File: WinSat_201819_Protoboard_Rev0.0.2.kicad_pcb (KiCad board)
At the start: 4 copper layers, 41 x 62 mm, 63 parts, among them J1 Conn_01x02_Female, J2 Conn_01x02_Female, J3 Conn_01x02_Female, J4 Conn_01x02_Female, J5 Conn_01x03_Female, J6 Conn_01x02_Female, J7 JTAG-6PIN, J8 Conn_01x03_Female, P1 TPS82150, Q1 SSM3K329R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

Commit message: Added GPS JST
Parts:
- added J9: Conn_01x04, Connector_JST:JST_PH_B4B-PH-K_1x04_P2.00mm_Vertical, F.Cu at (87.0, 100.0)
- added MK1: Mounting_Hole, MountingHole:MountingHole_3.2mm_M3, F.Cu at (68.0, 124.0)
- added MK2: Mounting_Hole, MountingHole:MountingHole_3.2mm_M3, F.Cu at (100.5, 70.5)
- added MK3: Mounting_Hole, MountingHole:MountingHole_3.2mm_M3, F.Cu at (101.0, 124.0)
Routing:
- net Net-(J9-Pad2): track 1.27 -> 10.5 mm
- net Net-(J9-Pad1): track 1.71 -> 7.97 mm
- net GND: track 120.6 -> 116.0 mm, vias 62 -> 63
- net +3V3: track 70.0 -> 71.5 mm, vias 20 -> 21

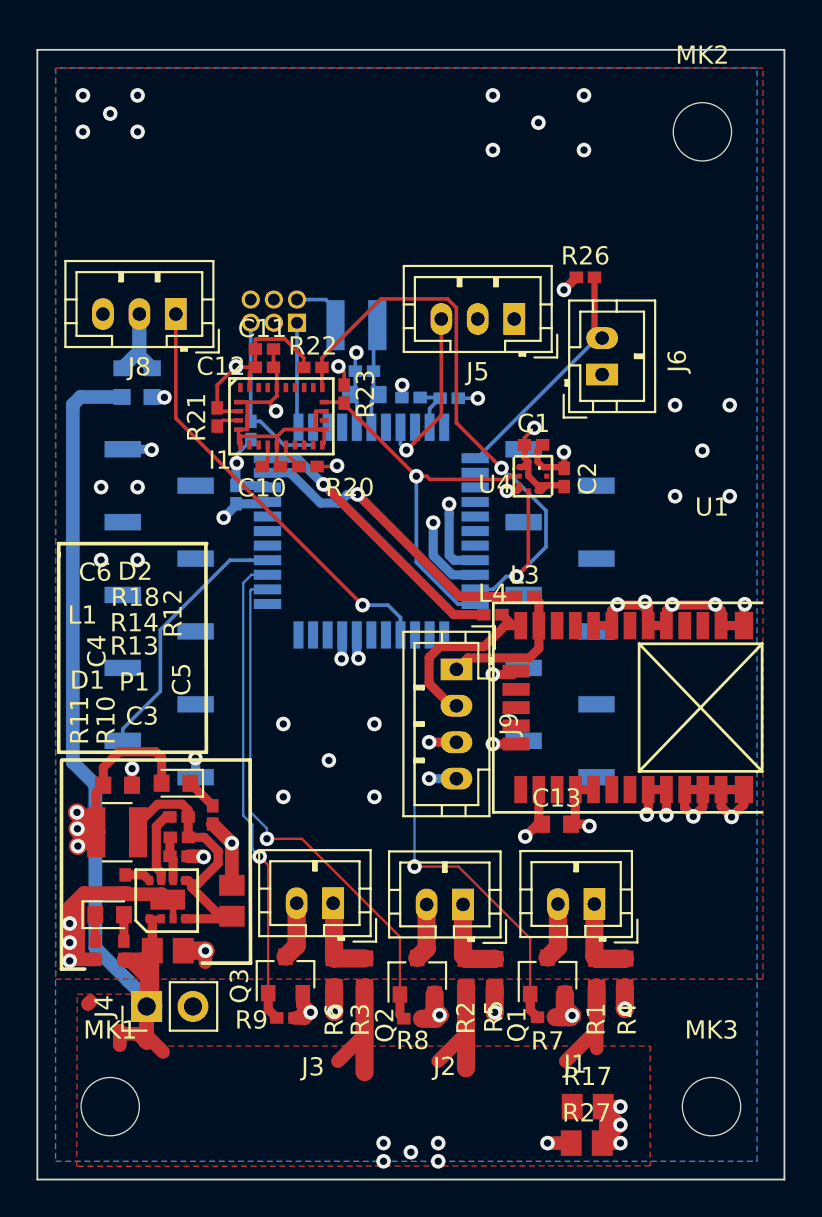
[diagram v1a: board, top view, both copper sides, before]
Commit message: GPS to 3 pin and board shrinkage
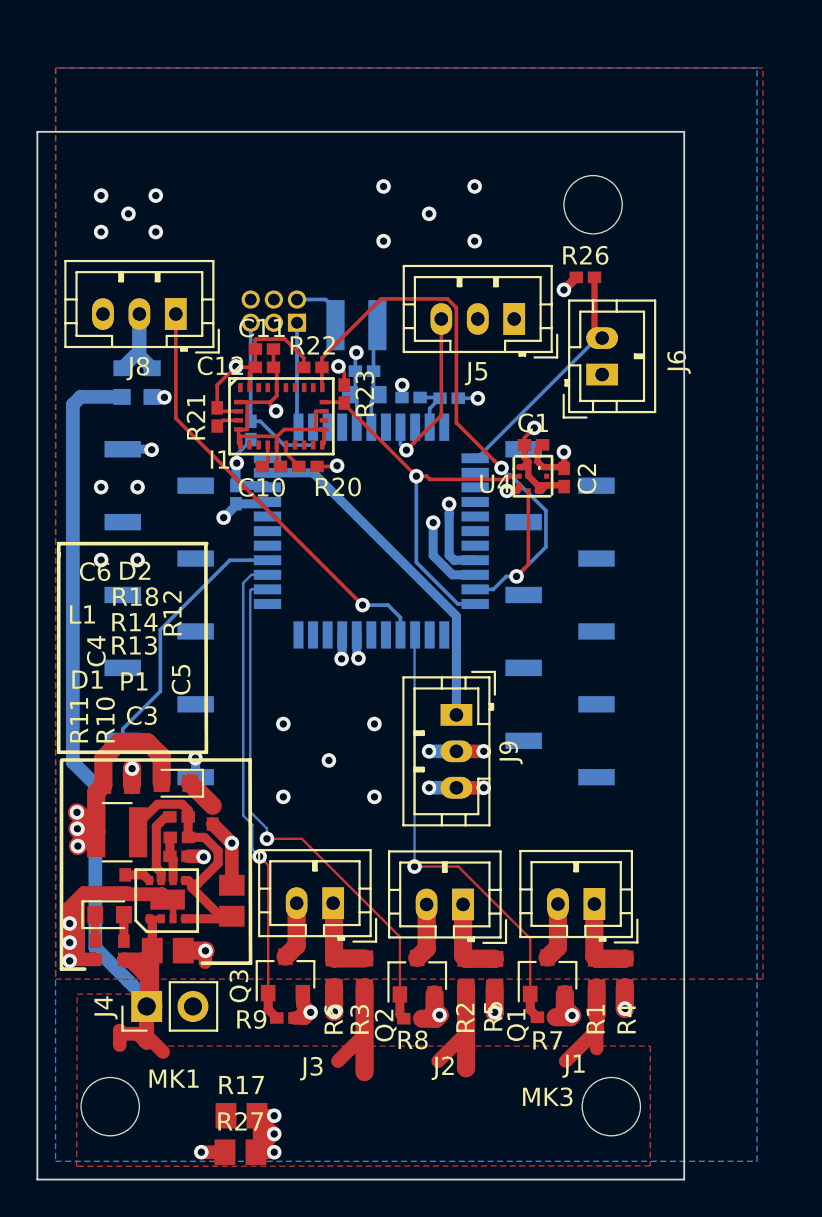
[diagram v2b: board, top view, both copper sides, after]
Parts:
- removed C13: 4.7uF, Capacitor_SMD:C_0603_1608Metric
- removed L3: L_Small, OSD335x-KiCad-master:Not_Broken_0402
- removed L4: BLM15HD102SN1, OSD335x-KiCad-master:Not_Broken_0402
- removed U1: CAM-M8, OSD335x-KiCad-master:CAM-M8
- J9: value Conn_01x04 -> Conn_01x03_Female; footprint Connector_JST:JST_PH_B4B-PH-K_1x04_P2.00mm_Vertical -> Connector_JST:JST_PH_B3B-PH-K_1x03_P2.00mm_Vertical
- moved R17 19.0 mm to (75.2, 124.5)
- moved R27 19.0 mm to (75.2, 126.5)
- moved MK2 7.21 mm to (94.5, 74.5)
- moved MK3 5.50 mm to (95.5, 124.0)
- moved J9 2.50 mm to (87.0, 102.5)
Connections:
- J9 pad 1: Net-(J9-Pad1) -> GPS_TX-MCU_RX
- J9 pad 2: Net-(J9-Pad2) -> GND
- U9 pad 33: GPS_RX-MCU_TX -> Net-(U9-Pad33)
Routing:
- net GND: track 116.0 -> 86.0 mm, vias 63 -> 44
- net GPS_RX-MCU_TX: track 15.4 -> 0.00 mm, vias 1 -> 0
- net Net-(J9-Pad2): track 10.5 -> 0.00 mm
- net Net-(J9-Pad1): track 7.97 -> 0.00 mm
- net +3V3: track 71.5 -> 66.8 mm, vias 21 -> 19
- net GPS_TX-MCU_RX: track 16.8 -> 19.0 mm, vias 1 -> 0
- net Net-(D2-Pad1): track 1.75 -> 3.49 mm
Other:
- board size 41 x 62 mm -> 35.5 x 57.5 mm

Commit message: FTDI Added
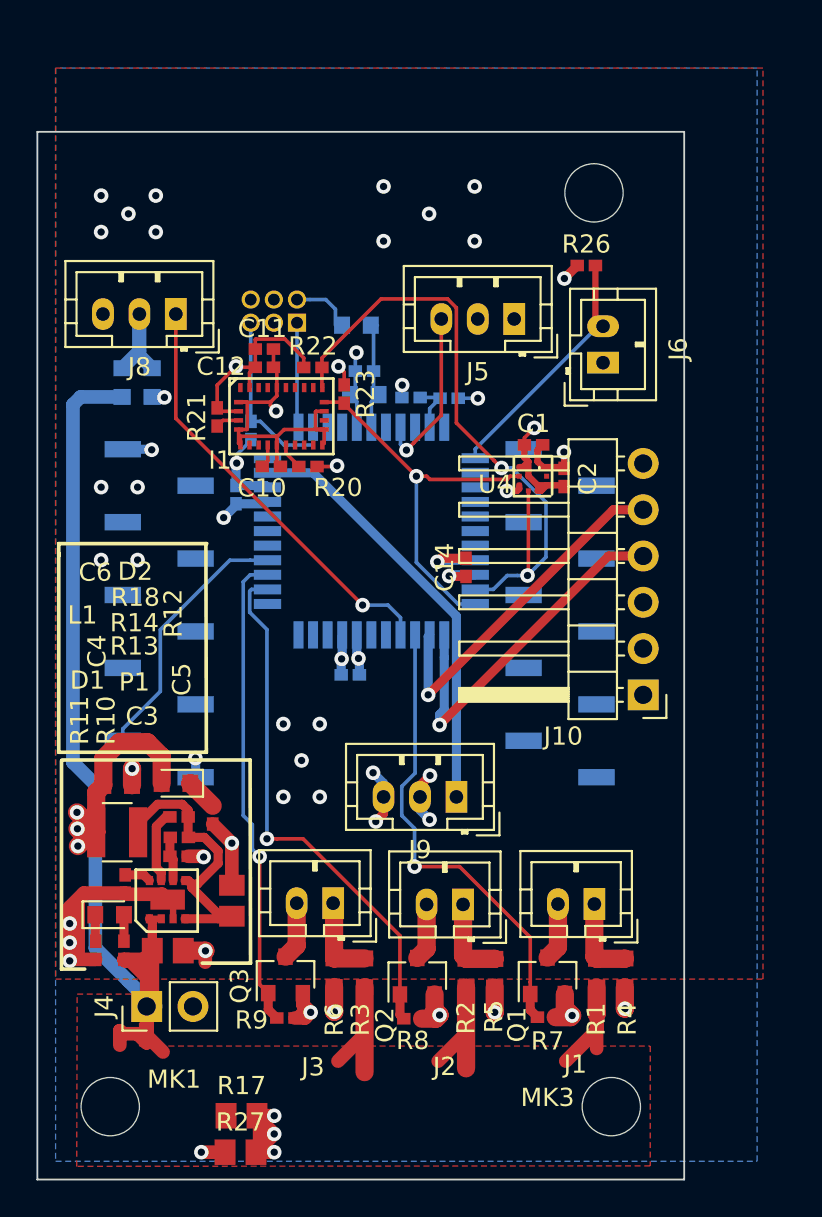
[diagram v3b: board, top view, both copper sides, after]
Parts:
- added C13: C_Small, OSD335x-KiCad-master:Not_Broken_0402, B.Cu at (81.2, 100.3)
- added C14: C_Small, OSD335x-KiCad-master:Not_Broken_0402, F.Cu at (87.5, 94.4)
- added J10: Conn_01x06_Male, Connector_PinHeader_2.54mm:PinHeader_1x06_P2.54mm_Horizontal, F.Cu at (97.2, 101.4)
- L2: value 10uH -> 220OHM 100MHZ; footprint Inductor_SMD:L_Abracon_ASPI-3012S -> Inductor_SMD:L_0603_1608Metric
- moved J9 4.50 mm to (87.0, 107.0), turned to 180 degrees
- moved MK2 0.65 mm to (94.5, 73.8)
- moved R26 0.65 mm to (94.1, 77.8)
- moved J6 0.65 mm to (95.0, 83.2)
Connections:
- U9 pad 12: Net-(U9-Pad12) -> FTDI_OLOG_TX-MCU_RX
- U9 pad 13: Net-(U9-Pad13) -> FTDI_OLOG_RX-MCU_TX
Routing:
- net FTDI_OLOG_TX-MCU_RX: track 0.00 -> 20.1 mm, vias 0 -> 1
- net FTDI_OLOG_RX-MCU_TX: track 0.00 -> 19.3 mm, vias 0 -> 1
- net GPS_TX-MCU_RX: track 19.0 -> 23.5 mm
- net +3V3: track 66.8 -> 65.6 mm
- net TEMP_SENSE-ADC: track 13.2 -> 13.9 mm
- net MOSFET0_GPIO: track 25.2 -> 25.8 mm

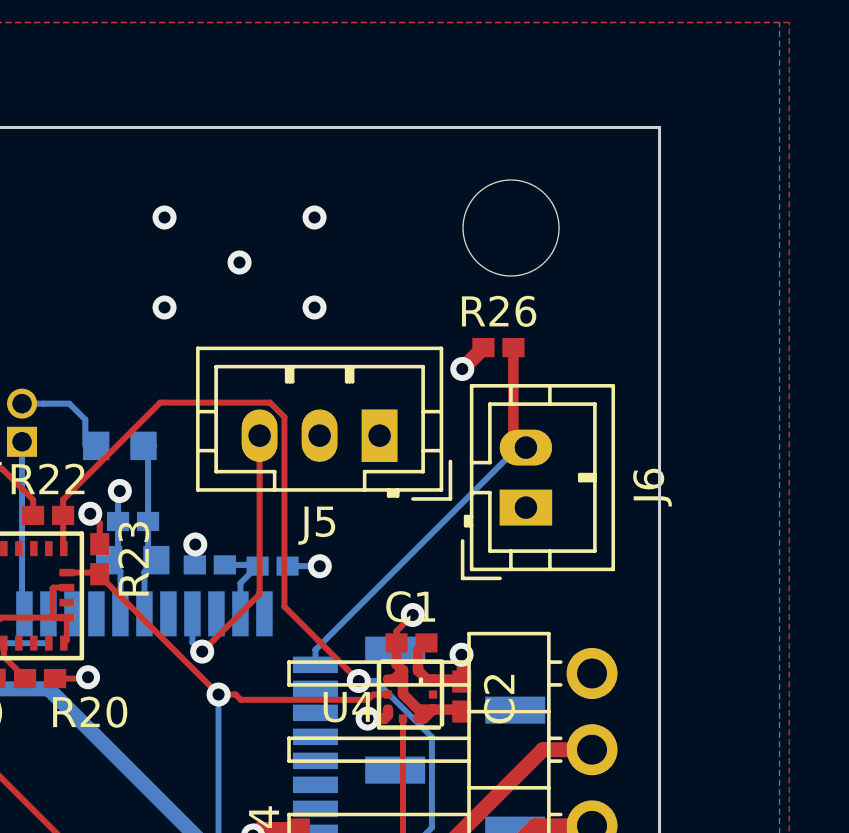
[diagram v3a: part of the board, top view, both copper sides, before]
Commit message: Fix mounting hole position
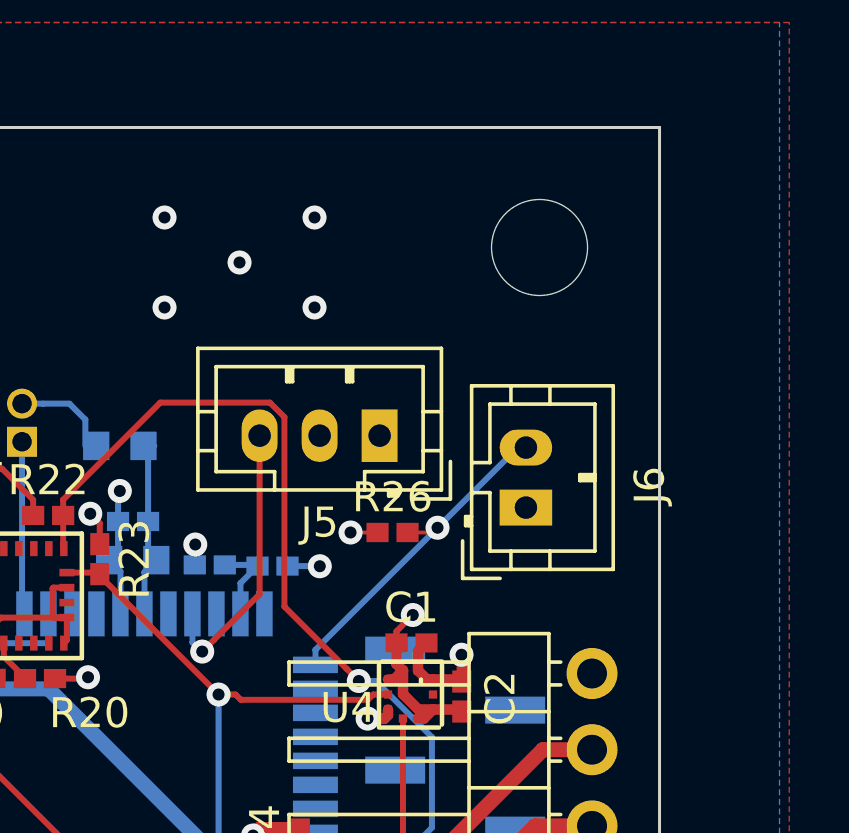
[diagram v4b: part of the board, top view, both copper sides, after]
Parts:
- moved R26 7.10 mm to (90.6, 84.0)
- moved MK2 1.15 mm to (95.5, 74.5)
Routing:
- net TEMP_SENSE-ADC: track 13.9 -> 12.1 mm, vias 0 -> 1
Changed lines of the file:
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@@
-(kicad_pcb (version 20171130) (host pcbnew "(5.0.0-rc2-129-g72b49accc)")
+(kicad_pcb (version 20171130) (host pcbnew "(5.0.0-3-g5ebb6b6)")
   (general
     (thickness 1.6)
     (drawings 15)
-    (tracks 506)
+    (tracks 508)
     (zones 0)
     (modules 66)
@@
   )
   (setup
-    (last_trace_width 0.5)
+    (last_trace_width 0.13)
     (user_trace_width 0.13)
     (user_trace_width 0.2)
@@
   )
   (module MountingHole:MountingHole_3.2mm_M3 (layer F.Cu)
-    (at 94.55 73.85)
+    (at 95.5 74.5)
     (descr "Mounting Hole 3.2mm, no annular, M3")
     (tags "mounting hole 3.2mm no annular m3")
@@
   )
   (module OSD335x-KiCad-master:Not_Broken_0402 (layer F.Cu)
-    (at 94.128 77.836)
+    (at 90.6 84)
     (descr "Resistor SMD 0402 (1005 Metric), square (rectangular) end terminal, IPC_7351 nominal, (Body size source: http://www.tortai-tech.com/upload/download/2011102023233369053.pdf), generated with kicad-footprint-generator")
     (tags resistor)
@@
   (segment (start 92.91 88.97) (end 92.91 88.085) (width 0.35) (layer F.Cu) (net 5))
   (segment (start 92.91 88.085) (end 92.9 88.075) (width 0.35) (layer F.Cu) (net 5))
-  (segment (start 93.628 77.836) (end 93.628 77.847) (width 0.5) (layer F.Cu) (net 5))
-  (segment (start 93.628 77.847) (end 92.95 78.525) (width 0.5) (layer F.Cu) (net 5))
   (segment (start 81.450738 84.624848) (end 81.153238 84.922348) (width 0.2) (layer B.Cu) (net 5))
   (segment (start 81.450738 83.632348) (end 81.450738 84.624848) (width 0.2) (layer B.Cu) (net 5))
@@
   (segment (start 85 107) (end 85 106.375) (width 0.5) (layer F.Cu) (net 5))
   (segment (start 85 106.375) (end 85.55 105.825) (width 0.5) (layer F.Cu) (net 5))
-  (via (at 92.925 78.55) (size 0.8) (drill 0.4) (layers F.Cu B.Cu) (net 5))
   (via (at 85.95 94.1) (size 0.8) (drill 0.4) (layers F.Cu B.Cu) (net 5))
   (segment (start 86.037652 94.012348) (end 85.95 94.1) (width 0.5) (layer B.Cu) (net 5))
@@
   (segment (start 86.15 93.9) (end 85.95 94.1) (width 0.5) (layer F.Cu) (net 5))
   (segment (start 87.525 93.9) (end 86.15 93.9) (width 0.5) (layer F.Cu) (net 5))
+  (via (at 89.2 84) (size 0.8) (drill 0.4) (layers F.Cu B.Cu) (net 5))
+  (segment (start 90.1 84) (end 89.2 84) (width 0.13) (layer F.Cu) (net 5))
   (segment (start 83.9 118.96198) (end 84.1124 119.17438) (width 0.5) (layer F.Cu) (net 6))
   (segment (start 83.9 117.84) (end 83.9 118.96198) (width 0.5) (layer F.Cu) (net 6))
@@
   (segment (start 70.8 111.59) (end 70.8 111.153602) (width 0.5) (layer F.Cu) (net 13))
   (segment (start 94.628 80.752) (end 95.046 81.17) (width 0.35) (layer F.Cu) (net 14))
-  (segment (start 94.628 77.836) (end 94.628 80.752) (width 0.35) (layer F.Cu) (net 14))
   (segment (start 88.128652 88.412348) (end 88.030738 88.412348) (width 0.2) (layer B.Cu) (net 14))
   (segment (start 88.030738 87.910262) (end 88.030738 88.412348) (width 0.2) (layer B.Cu) (net 14))
   (segment (start 95.046 81.17) (end 94.771 81.17) (width 0.2) (layer B.Cu) (net 14))
-  (segment (start 94.771 81.17) (end 88.030738 87.910262) (width 0.2) (layer B.Cu) (net 14))
+  (via (at 92.1 83.841) (size 0.8) (drill 0.4) (layers F.Cu B.Cu) (net 14))
+  (segment (start 91.1 84) (end 91.941 84) (width 0.13) (layer F.Cu) (net 14))
+  (segment (start 92.1 83.841) (end 88.030738 87.910262) (width 0.2) (layer B.Cu) (net 14))
+  (segment (start 91.941 84) (end 92.1 83.841) (width 0.13) (layer F.Cu) (net 14))
+  (segment (start 94.771 81.17) (end 92.1 83.841) (width 0.2) (layer B.Cu) (net 14))
   (segment (start 77.64382 88.13718) (end 77.64382 87.68718) (width 0.2) (layer F.Cu) (net 15))
   (segment (start 78.35 88.84336) (end 77.64382 88.13718) (width 0.2) (layer F.Cu) (net 15))
